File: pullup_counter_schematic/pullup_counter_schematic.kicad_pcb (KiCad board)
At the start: 2 copper layers, 75 x 45 mm, 53 parts, among them J1 FOUR_WIRE_CONN, J2 READ_PORT, Q1 MMBT3904, Q2 MMBT3904, Q3 MMBT3904, Q4 MMBT3906, SW1 SW_Push, U1 LM358, U2 HT7333, U3 P25Q40H, U4 dual_sev_seg_display, U5 AT24C02, U6 STM32F031C6Tx, Y1 32.768KHz

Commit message: Created PCB
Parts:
- removed JP1: Jumper_2_Open, Jumper:SolderJumper-2_P1.3mm_Open_RoundedPad1.0x1.5mm
- removed JP2: Jumper_3_Open, Connector_PinSocket_2.54mm:PinSocket_1x03_P2.54mm_Vertical
- removed RN1: Voltage_Divider, Potentiometer_THT:Potentiometer_Piher_PT-10-V05_Vertical
- added BT3: CR2032, Battery_Custom:CR2032_CR2025_Battery_Holder, F.Cu at (113.0, 60.0)
- added C13: 100nF, Capacitor_SMD:C_0805_2012Metric_Pad1.18x1.45mm_HandSolder, F.Cu at (125.5, 81.0)
- added C14: 100nF, Capacitor_SMD:C_0805_2012Metric_Pad1.18x1.45mm_HandSolder, F.Cu at (136.5, 82.5)
- added C15: 4.7uF, Capacitor_SMD:C_0805_2012Metric_Pad1.18x1.45mm_HandSolder, F.Cu at (137.0, 70.0)
- added C16: 1uF, Capacitor_SMD:C_0805_2012Metric_Pad1.18x1.45mm_HandSolder, F.Cu at (151.8, 95.0)
- added C17: 10pF, Capacitor_SMD:C_0603_1608Metric_Pad1.08x0.95mm_HandSolder, F.Cu at (139.0, 80.4)
- added C18: 10pF, Capacitor_SMD:C_0603_1608Metric_Pad1.08x0.95mm_HandSolder, F.Cu at (139.0, 76.1)
- added D1: D_Schottky, Diode_SMD:D_SMA_Handsoldering, F.Cu at (127.5, 48.5)
- added Q5: MMBT3906, Package_TO_SOT_SMD:SOT-23_Handsoldering, F.Cu at (145.0, 88.0)
- added R19: 47K, Resistor_SMD:R_0805_2012Metric_Pad1.20x1.40mm_HandSolder, F.Cu at (113.5, 95.0)
- added R20: 47K, Resistor_SMD:R_0805_2012Metric_Pad1.20x1.40mm_HandSolder, F.Cu at (116.5, 95.0)
- added R21: R, Resistor_SMD:R_0805_2012Metric_Pad1.20x1.40mm_HandSolder, F.Cu at (140.0, 86.5)
- added R22: R, Resistor_SMD:R_0805_2012Metric_Pad1.20x1.40mm_HandSolder, F.Cu at (140.5, 91.0)
- added R23: R, Resistor_SMD:R_0805_2012Metric_Pad1.20x1.40mm_HandSolder, F.Cu at (149.0, 93.0)
- added SW2: rst, custom_buttons_switches:TSB008, F.Cu at (125.7, 89.5)
- added SW3: start, custom_buttons_switches:TSB008, F.Cu at (131.7, 89.5)
- added SW4: TouchPad, TouchPad:TouchPad_100x100, F.Cu at (168.9, 93.3)
- added U7: STM32L051C8Tx, Package_QFP:LQFP-48_7x7mm_P0.5mm, F.Cu at (132.0, 76.0)
- added U8: KTIR0711S, pullup_counter_schematic:KTIR0711S, F.Cu at (142.7, 95.4)
- BT1: value Battery -> LR03; footprint Connector_PinHeader_2.54mm:PinHeader_1x02_P2.54mm_Vertical -> Battery_Custom:SMD_SMT_AAA_LR03; moved to B.Cu
- BT2: value Battery_Cell -> LR03; footprint Battery_Custom:CR2032_CR2025_Battery_Holder -> Battery_Custom:SMD_SMT_AAA_LR03
- C1, C5: value 1uF -> 10uF; footprint Capacitor_SMD:C_1206_3216Metric_Pad1.33x1.80mm_HandSolder -> Capacitor_SMD:C_0805_2012Metric_Pad1.18x1.45mm_HandSolder
- C10: value 10pF -> ?pF; footprint Capacitor_SMD:C_0603_1608Metric_Pad1.08x0.95mm_HandSolder -> Capacitor_SMD:C_0805_2012Metric_Pad1.18x1.45mm_HandSolder
- C11: value 10pF -> 1uF; footprint Capacitor_SMD:C_0603_1608Metric_Pad1.08x0.95mm_HandSolder -> Capacitor_SMD:C_0805_2012Metric_Pad1.18x1.45mm_HandSolder
- C12, C3, C4: footprint Capacitor_SMD:C_1206_3216Metric_Pad1.33x1.80mm_HandSolder -> Capacitor_SMD:C_0805_2012Metric_Pad1.18x1.45mm_HandSolder
- C2: value 10uF -> 100nF; footprint Capacitor_SMD:C_1206_3216Metric_Pad1.33x1.80mm_HandSolder -> Capacitor_SMD:C_0805_2012Metric_Pad1.18x1.45mm_HandSolder
- C6: value 1uF -> 100nF; footprint Capacitor_SMD:C_1206_3216Metric_Pad1.33x1.80mm_HandSolder -> Capacitor_SMD:C_0805_2012Metric_Pad1.18x1.45mm_HandSolder
- C7, C8: value 100nF -> 10uF; footprint Capacitor_SMD:C_1206_3216Metric_Pad1.33x1.80mm_HandSolder -> Capacitor_SMD:C_0805_2012Metric_Pad1.18x1.45mm_HandSolder
- C9: value 4.7uF -> 100nF; footprint Capacitor_SMD:C_1206_3216Metric_Pad1.33x1.80mm_HandSolder -> Capacitor_SMD:C_0805_2012Metric_Pad1.18x1.45mm_HandSolder
- J1: value FOUR_WIRE_CONN -> USB_B_Micro; footprint Connector_PinHeader_2.54mm:PinHeader_1x04_P2.54mm_Vertical -> Connector_USB:USB_Micro-B_Amphenol_10118194_Horizontal
- J2: value READ_PORT -> 6PinDebugPort; footprint Connector_PinSocket_2.54mm:PinSocket_2x03_P2.54mm_Vertical -> Connector_IDC:IDC-Header_2x03_P2.54mm_Vertical; moved to F.Cu
- Q1, Q2: footprint Package_TO_SOT_SMD:SOT-23 -> Package_TO_SOT_SMD:SOT-23_Handsoldering
- Q3, Q4: footprint Package_TO_SOT_SMD:SOT-23 -> Package_TO_SOT_SMD:SOT-23_Handsoldering; moved to F.Cu
- R1: value 10K -> 1K
- R12: value 1K2 -> 10K
- R13: value R -> 10K
- R14: value R -> 1K2
- R15, R16, R17, R3, R4, R5, R6, R7: moved to F.Cu
- R18: value 10K -> 47K
- R2: value R_PHOTO -> 1K; footprint OptoDevice:R_LDR_5.0x4.1mm_P3mm_Vertical -> Resistor_SMD:R_0805_2012Metric_Pad1.20x1.40mm_HandSolder
- R8, R9: value 1K -> 220R; moved to F.Cu
- SW1: value SW_Push -> boot
- U1: value LM358 -> COM_C; footprint Package_SO:SOIC-8_3.9x4.9mm_P1.27mm -> Seven_Segment_Display_Custom:2_Digit_0_56_inch
- U2: value HT7333 -> HT7325
- U3: value P25Q40H -> CH340C; footprint Package_SO:SOIC-8_3.9x4.9mm_P1.27mm -> Package_SO:SOIC-16_3.9x9.9mm_P1.27mm
- U4: value dual_sev_seg_display -> HT7325; footprint Seven_Segment_Display_Custom:2_Digit_0_56_inch -> Package_TO_SOT_SMD:SOT-89-3
- U5: value AT24C02 -> P25Q40H
- U6: value STM32F031C6Tx -> TTP223; footprint Package_QFP:LQFP-48_7x7mm_P0.5mm -> Package_TO_SOT_SMD:TSOT-23-6
- moved H1 133.5 mm to (100.0, 92.5)
- moved C6 109.4 mm to (112.0, 80.5), turned to 270 degrees
- moved C5 101.0 mm to (109.5, 80.5), turned to 270 degrees
- moved R18 100.5 mm to (110.5, 95.0), turned to 90 degrees
- moved SW1 87.5 mm to (123.2, 95.5), turned to 90 degrees
- moved C7 86.7 mm to (118.6, 40.1), turned to 270 degrees
- moved R12 81.6 mm to (126.0, 86.0)
- moved C12 81.3 mm to (126.0, 71.0), turned to 180 degrees
- moved U5 80.6 mm to (132.5, 60.5), turned to 90 degrees
- moved R10 78.9 mm to (120.3, 86.0)
- moved C11 78.0 mm to (131.5, 54.5), turned to 0 degrees
- moved C8 76.6 mm to (129.1, 40.1)
- moved Y1 76.4 mm to (143.0, 80.9)
- moved BT1 68.9 mm to (109.0, 93.0), turned to 0 degrees
- moved C9 65.9 mm to (126.6, 40.1), turned to 270 degrees
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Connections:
- BT1 pad 2: GND -> Net-(BT1-Pad2)
- BT2 pad 1: +3V0 -> Net-(BT1-Pad2)
- C1 pad 1: +3V3 -> +5V
- C11 pad 1: Net-(C11-Pad1) -> VCC
- C12 pad 1: +3V0 -> VCC
- C2 pad 1: +BATT -> +5V
- C3 pad 1: +3V3 -> +BATT
- C4 pad 1: +3V3 -> Net-(C4-Pad1)
- C5 pad 1: /~HOLD -> VCC
- C6 pad 1: +3V3 -> VCC
- C7 pad 1: +3V3 -> +3V0
- C8 pad 1: +3V3 -> /V_BACKUP
- C9 pad 1: +3V3 -> /V_BACKUP
- J1 pad 1: GND -> +5V
- J1 pad 2: /SWCLK -> Net-(J1-Pad2)
- J1 pad 3: /SWDIO -> Net-(J1-Pad3)
- J1 pad 4: +3V3 -> GND
- J2 pad 1: /READ_PWR -> GND
- J2 pad 2: /MOSI -> /SWCLK
- J2 pad 3: /~CE -> /SWDIO
- J2 pad 4: /SCK -> /~RST
- J2 pad 5: /MISO -> (no net)
- J2 pad 6: GND -> VCC
- Q4 pad 2: Net-(Q4-Pad2) -> +BATT
- Q4 pad 3: +BATT -> Net-(Q4-Pad3)
- R1 pad 1: +3V3 -> Net-(R1-Pad1)
- R1 pad 2: /DIST_OUTA -> /dis_a
- R12 pad 1: Net-(Q2-Pad1) -> VCC
- R12 pad 2: /dis_sel_0 -> /~RST
- R13 pad 1: Net-(R13-Pad1) -> VCC
- R13 pad 2: /DIST_REF -> /Start
- R14 pad 1: /DIST_OUTD -> Net-(Q2-Pad1)
- R14 pad 2: Net-(R13-Pad1) -> /dis_sel_0
- R15 pad 1: Net-(Q3-Pad1) -> +5V
- R15 pad 2: /BAT_SENSE_EN -> /USB_FLAG
- R16 pad 1: /BAT_SENSE -> /USB_FLAG
- R16 pad 2: Net-(Q4-Pad2) -> GND
- R17 pad 1: GND -> Net-(Q3-Pad1)
- R17 pad 2: /BAT_SENSE -> /BAT_SENSE_EN
- R18 pad 1: +3V3 -> +BATT
- R18 pad 2: /~RST -> Net-(Q3-Pad3)
- R2 pad 1: /DIST_OUTA -> Net-(R2-Pad1)
- R2 pad 2: GND -> /dis_b
- R3 pad 2: /dis_a -> /dis_c
- R4 pad 2: /dis_b -> /dis_d
- R5 pad 2: /dis_c -> /dis_e
- R6 pad 2: /dis_d -> /dis_f
- R7 pad 2: /dis_e -> /dis_g
- R8 pad 1: Net-(R8-Pad1) -> Net-(J1-Pad3)
- R8 pad 2: /dis_f -> /USB_DP
- R9 pad 1: Net-(R9-Pad1) -> /USB_DM
- R9 pad 2: /dis_g -> Net-(J1-Pad2)
- SW1 pad 1: /~RST -> VCC
- SW1 pad 2: GND -> /boot
- U1 pad 1: /DIST_OUTD -> Net-(R3-Pad1)
- U1 pad 2: /DIST_OUTA -> (no net)
- U1 pad 3: Net-(R13-Pad1) -> Net-(R5-Pad1)
- U1 pad 4: GND -> Net-(R4-Pad1)
- U1 pad 5: GND -> Net-(R7-Pad1)
- U1 pad 6: GND -> Net-(R6-Pad1)
- U1 pad 7: (no net) -> /disp_pwr_0
- U1 pad 8: +3V3 -> /disp_pwr_1
- U2 pad 3: +3V3 -> VCC
- U3 pad 1: /~CE -> GND
- U3 pad 2: /MISO -> /MCU_RX
- U3 pad 3: /~HOLD -> /MCU_TX
- U3 pad 4: GND -> Net-(C4-Pad1)
- U3 pad 5: /MOSI -> /USB_DP
- U3 pad 6: /SCK -> /USB_DM
- U3 pad 7: /~HOLD -> (no net)
- U3 pad 8: /~HOLD -> (no net)
- U4 pad 1: Net-(R5-Pad1) -> GND
- U4 pad 2: (no net) -> +3V0
- U4 pad 3: Net-(R7-Pad1) -> /V_BACKUP
- U5 pad 1: GND -> /~CE
- U5 pad 2: GND -> /MISO
- U5 pad 3: GND -> VCC
- U5 pad 5: /SDA -> /MOSI
- U5 pad 6: /SCL -> /SCK
- U5 pad 7: GND -> VCC
- U5 pad 8: +3V3 -> VCC
- U6 pad 1: +3V0 -> /TouchPin
- U6 pad 2: (no net) -> GND
- U6 pad 4: Net-(C11-Pad1) -> GND
- U6 pad 5: (no net) -> VCC
- U6 pad 6: (no net) -> GND
- Y1 pad 1: Net-(C10-Pad1) -> Net-(C17-Pad1)
- Y1 pad 2: Net-(C11-Pad1) -> Net-(C18-Pad1)
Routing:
- net VCC: track 0.00 -> 193.1 mm, vias 0 -> 5
- net +3V3: track 154.5 -> 0.00 mm, vias 2 -> 0
- net /dis_sel_0: track 25.2 -> 84.3 mm, vias 0 -> 2
- net /dis_f: track 20.6 -> 74.5 mm, vias 1 -> 2
- net /~RST: track 18.7 -> 69.5 mm, vias 4 -> 3
- net Net-(BT1-Pad2): track 0.00 -> 50.6 mm
- net /~HOLD: track 46.2 -> 0.00 mm, vias 2 -> 0
- net /dis_sel_1: track 31.9 -> 77.8 mm, vias 0 -> 2
- net /dis_g: track 19.6 -> 62.2 mm, vias 1 -> 2
- net /dis_b: track 29.2 -> 70.4 mm, vias 1 -> 2
- net /USB_FLAG: track 0.00 -> 40.7 mm, vias 0 -> 2
- net /dis_d: track 22.4 -> 58.6 mm, vias 1 -> 2
- net /dis_a: track 31.2 -> 66.1 mm, vias 1 -> 2
- net /MISO: track 42.9 -> 9.69 mm, vias 3 -> 0
- net /TouchPin: track 0.00 -> 32.7 mm, vias 0 -> 4
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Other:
- board size 75 x 45 mm -> 95 x 65 mm
- board text added: "BOOT"
- board text added: "Otwory M3"
- board text added: "START"
- board text removed: "+ -"
- board text removed: "Debug Port"
- board text removed: "Flash Read Port"
- board text removed: "GND"
- board text removed: "JLCJLCJLCJLC"
- board text removed: "MOSI/SCK/GND VCC/~CE~/MISO"
- board text removed: "Normal Operation"
- board text removed: "Pull-up Counter - v01 - by Mkrysz"
- board text removed: "Read Data"
- board text removed: "SWCLK"
- board text removed: "SWDIO"
- board text removed: "VCC"
- board text removed: "boot jumper"

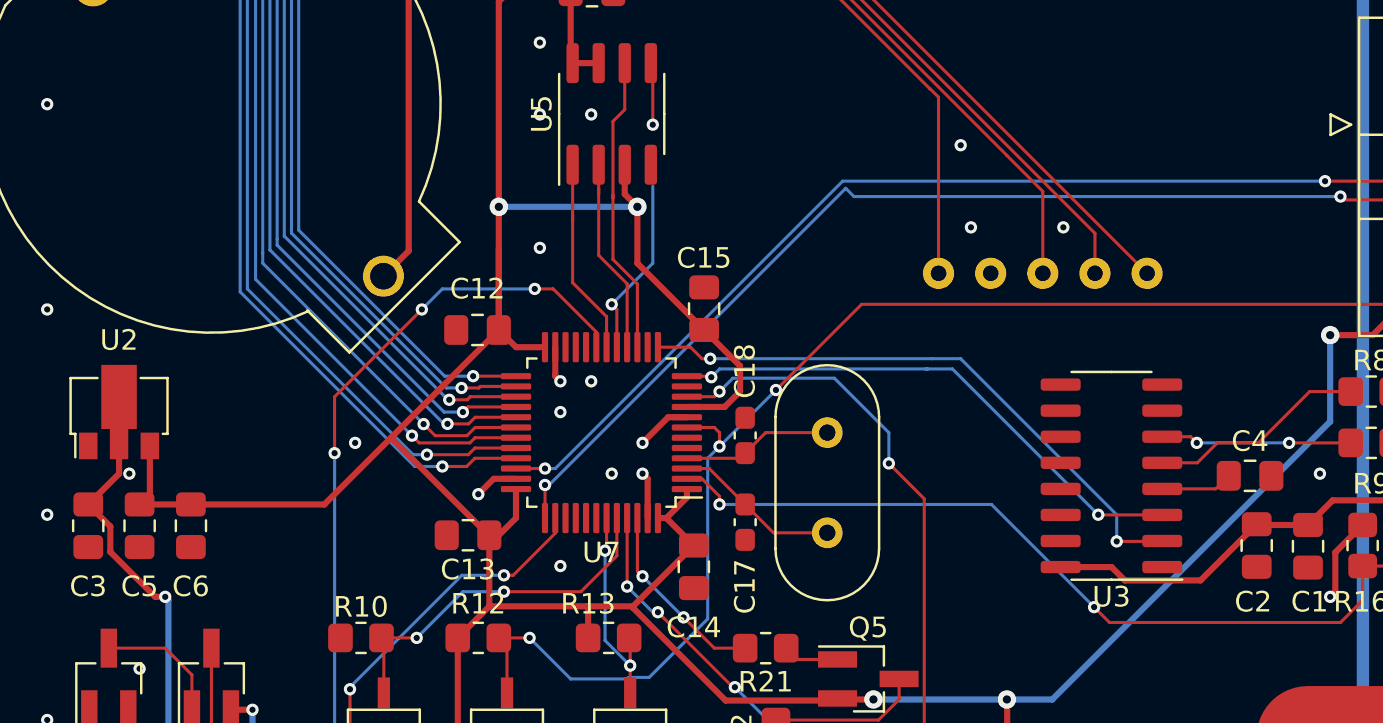
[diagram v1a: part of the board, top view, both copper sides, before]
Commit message: Runned DRC and fixed some problems
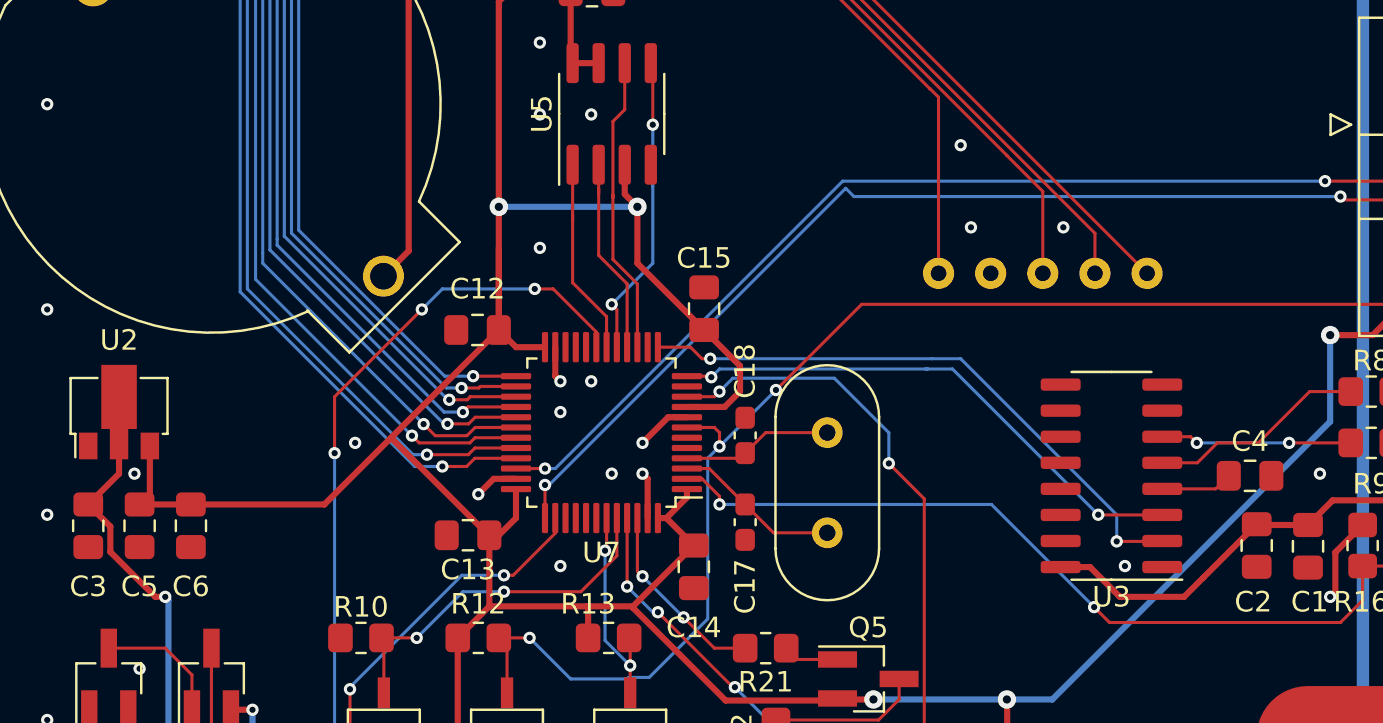
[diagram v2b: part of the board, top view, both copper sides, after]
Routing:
- net /MOSI: track 11.8 -> 14.8 mm
- net +5V: track 23.6 -> 24.3 mm
- net GND: vias 38 -> 39

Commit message: Generated PCB's Gerbers
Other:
- board text added: "JLCJLCJLCJLC"
- board text added: "Pull-up Counter V02 By MKrysz"

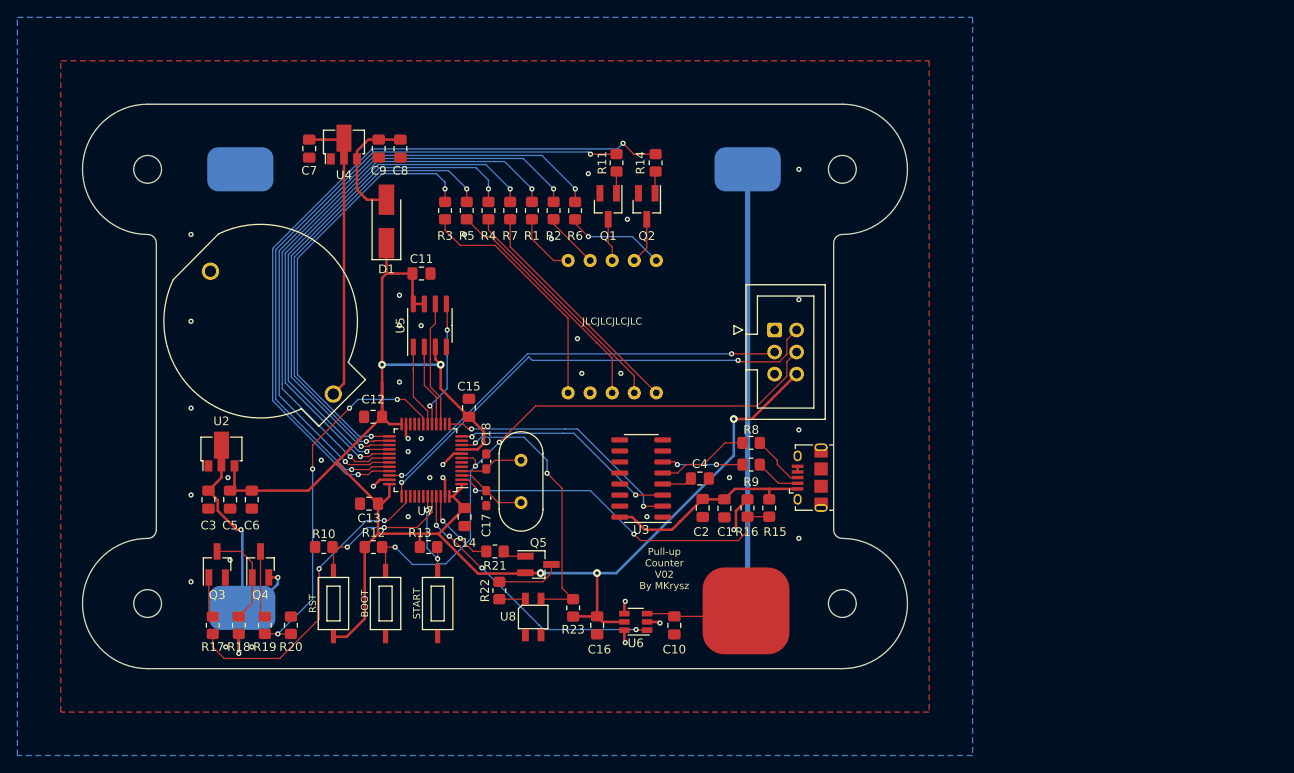
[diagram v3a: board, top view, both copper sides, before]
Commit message: Added step-up, SD-Card, OLED display and changed MCU
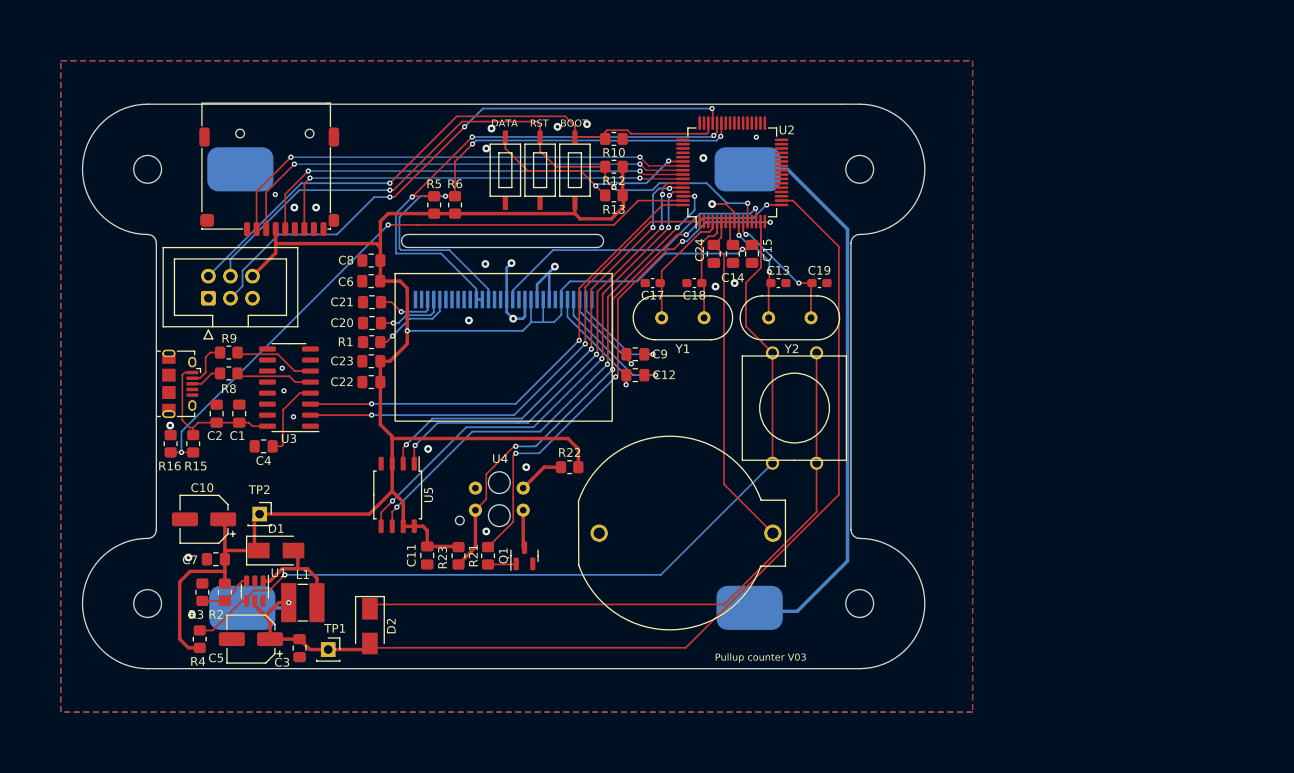
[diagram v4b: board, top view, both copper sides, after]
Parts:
- removed C16: 1uF, Capacitor_SMD:C_0805_2012Metric_Pad1.18x1.45mm_HandSolder
- removed Q2, Q3: MMBT3904, Package_TO_SOT_SMD:SOT-23_Handsoldering
- removed Q4, Q5: MMBT3906, Package_TO_SOT_SMD:SOT-23_Handsoldering
- removed R11, R14: 1K2, Resistor_SMD:R_0805_2012Metric_Pad1.20x1.40mm_HandSolder
- removed R17, R18, R19, R20: 47K, Resistor_SMD:R_0805_2012Metric_Pad1.20x1.40mm_HandSolder
- removed R7: 1K, Resistor_SMD:R_0805_2012Metric_Pad1.20x1.40mm_HandSolder
- removed U6: TTP223, Package_TO_SOT_SMD:TSOT-23-6
- removed U7: STM32L051C8Tx, Package_QFP:LQFP-48_7x7mm_P0.5mm
- removed U8: KTIR0711S, pullup_counter_schematic:KTIR0711S
- added C19: 20pF, Capacitor_SMD:C_0603_1608Metric_Pad1.08x0.95mm_HandSolder, F.Cu at (177.4, 55.6)
- added C20: 10uF, Capacitor_SMD:C_0805_2012Metric_Pad1.18x1.45mm_HandSolder, F.Cu at (125.8, 60.2)
- added C21: 10uF, Capacitor_SMD:C_0805_2012Metric_Pad1.18x1.45mm_HandSolder, F.Cu at (125.8, 57.8)
- added C22: 10uF, Capacitor_SMD:C_0805_2012Metric_Pad1.18x1.45mm_HandSolder, F.Cu at (125.8, 67.0)
- added C23: 100nF, Capacitor_SMD:C_0805_2012Metric_Pad1.18x1.45mm_HandSolder, F.Cu at (125.8, 64.6)
- added C24: 100nF, Capacitor_SMD:C_0805_2012Metric_Pad1.18x1.45mm_HandSolder, F.Cu at (165.2, 52.2)
- added D2: SS14, Diode_SMD:D_SMA, F.Cu at (125.6, 95.1)
- added DS1: OLED-128O064D, Display:OLED-128O064D, F.Cu at (141.0, 57.5)
- added J3: Micro_SD_Card, uSD_socket:uSD_socket, F.Cu at (117.0, 45.9)
- added L1: 4.7uH, Inductor_SMD:L_Ferrocore_DLG-0403, F.Cu at (117.9, 92.4)
- added TP1: ~, Connector_PinSocket_2.54mm:PinSocket_1x01_P2.54mm_Vertical, F.Cu at (120.8, 97.8)
- added TP2: ~, Connector_PinSocket_2.54mm:PinSocket_1x01_P2.54mm_Vertical, F.Cu at (112.9, 82.2)
- added Y2: 8MHz, Crystal:Crystal_HC49-4H_Vertical, F.Cu at (171.5, 59.6)
- C10: value ?pF -> 22uF; footprint Capacitor_SMD:C_0805_2012Metric_Pad1.18x1.45mm_HandSolder -> Capacitor_SMD:CP_Elec_5x4.5
- C12, C9: value 100nF -> 2.2uF
- C13: value 100nF -> 20pF; footprint Capacitor_SMD:C_0805_2012Metric_Pad1.18x1.45mm_HandSolder -> Capacitor_SMD:C_0603_1608Metric_Pad1.08x0.95mm_HandSolder
- C3, C7, C8: value 10uF -> 100nF
- C5: value 10uF -> 22uF; footprint Capacitor_SMD:C_0805_2012Metric_Pad1.18x1.45mm_HandSolder -> Capacitor_SMD:CP_Elec_5x4.5
- C6: value 100nF -> 10uF
- D1: value D_Schottky -> SS14; footprint Diode_SMD:D_SMA_Handsoldering -> Diode_SMD:D_SMA
- Q1: footprint Package_TO_SOT_SMD:SOT-23_Handsoldering -> Package_TO_SOT_SMD:SOT-23
- R1: value 1K -> 390K
- R2, R3: value 1K -> R
- R21: value R -> 1K2
- R22: value R -> 220R
- R23: value R -> 22K
- R4: value 1K -> 10K
- R5, R6: value 1K -> 4K7
- SW3: value start -> dataDump
- SW4: value TouchPad -> start; footprint TouchPad:TouchPad_100x100 -> custom_buttons_switches:sw_push_12_x_12_mm
- U1: value COM_C -> MT3608; footprint Seven_Segment_Display_Custom:2_Digit_0_56_inch -> Package_TO_SOT_SMD:SOT-23-6
- U2: value HT7325 -> STM32G070RBT6; footprint Package_TO_SOT_SMD:SOT-89-3 -> Package_QFP:LQFP-64_10x10mm_P0.5mm
- U4: value HT7325 -> TCRT5000; footprint Package_TO_SOT_SMD:SOT-89-3 -> TCRT5000:TCRT5000
- U5: value P25Q40H -> W25Q80; footprint Package_SO:SOIC-8_3.9x4.9mm_P1.27mm -> Package_SO:SOIC-8_5.275x5.275mm_P1.27mm
- moved J1 73.3 mm to (103.8, 67.2), turned to -90 degrees
- moved U2 67.0 mm to (167.3, 42.9)
- moved R16 66.8 mm to (102.7, 74.1)
- moved R15 66.7 mm to (105.2, 74.1)
- moved J2 65.3 mm to (107.0, 57.3), turned to 90 degrees
- moved R9 61.5 mm to (109.3, 63.6), turned to 180 degrees
- moved R8 60.7 mm to (109.3, 66.0), turned to 0 degrees
- moved R4 59.5 mm to (106.0, 96.6)
- moved R2 58.0 mm to (108.9, 91.2), turned to -90 degrees
- moved R10 57.7 mm to (153.7, 39.0), turned to 0 degrees
- moved SW1 57.1 mm to (151.0, 45.6)
- moved C2 57.0 mm to (107.9, 70.6), turned to 90 degrees
- moved C1 56.9 mm to (110.5, 70.6), turned to 90 degrees
- moved C10 55.5 mm to (106.5, 82.8), turned to 180 degrees
- moved C13 53.5 mm to (172.6, 55.6), turned to 0 degrees
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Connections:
- BT1 pad 1: +BATT -> /BAT_RAW
- BT3 pad 1: +3V0 -> +BATT
- C10 pad 1: Net-(C10-Pad1) -> VCC
- C12 pad 1: VCC -> Net-(C12-Pad1)
- C12 pad 2: GND -> Net-(C12-Pad2)
- C13 pad 1: VCC -> /OSC_IN
- C17 pad 1: Net-(C17-Pad1) -> /OSC32_IN
- C18 pad 1: Net-(C18-Pad1) -> /OSC32_OUT
- C3 pad 1: +BATT -> /BAT_RAW
- C5 pad 1: VCC -> /BAT_RAW
- C7 pad 1: +3V0 -> VCC
- C8 pad 1: /V_BACKUP -> VCC
- C9 pad 1: /V_BACKUP -> Net-(C9-Pad1)
- C9 pad 2: GND -> Net-(C9-Pad2)
- D1 pad 2: /V_BACKUP -> Net-(D1-Pad2)
- J2 pad 4: /~RST -> /~{RST}
- J2 pad 5: (no net) -> unconnected-(J2-Pad5)
- Q1 pad 3: /disp_pwr_1 -> Net-(Q1-Pad3)
- R1 pad 1: Net-(R1-Pad1) -> Net-(DS1-Pad26)
- R1 pad 2: /dis_a -> GND
- R10 pad 1: /boot -> /SWCLK
- R12 pad 2: /~RST -> /~{RST}
- R13 pad 2: /Start -> /dataDump
- R2 pad 1: Net-(R2-Pad1) -> VCC
- R2 pad 2: /dis_b -> /PWR_FB
- R21 pad 1: Net-(Q5-Pad1) -> Net-(Q1-Pad1)
- R21 pad 2: /DISTANCE_EN -> /PROX_EN
- R22 pad 2: Net-(Q5-Pad3) -> VCC
- R23 pad 2: /DISTANCE -> /PROX_OUT
- R3 pad 1: Net-(R3-Pad1) -> /PWR_FB
- R3 pad 2: /dis_c -> GND
- R4 pad 1: Net-(R4-Pad1) -> VCC
- R4 pad 2: /dis_d -> /PWR_EN
- R5 pad 1: Net-(R5-Pad1) -> VCC
- R5 pad 2: /dis_e -> /SDA
- R6 pad 1: Net-(R6-Pad1) -> VCC
- R6 pad 2: /dis_f -> /SCK
- SW1 pad 2: /boot -> /SWCLK
- SW2 pad 1: /~RST -> /~{RST}
- SW3 pad 1: /Start -> /dataDump
- SW4 pad 1: Net-(C10-Pad1) -> Net-(D2-Pad1)
- U1 pad 1: Net-(R3-Pad1) -> Net-(D1-Pad2)
- U1 pad 2: (no net) -> GND
- U1 pad 3: Net-(R5-Pad1) -> /PWR_FB
- U1 pad 4: Net-(R4-Pad1) -> /PWR_EN
- U1 pad 5: Net-(R7-Pad1) -> /BAT_RAW
- U1 pad 6: Net-(R6-Pad1) -> unconnected-(U1-Pad6)
- U2 pad 1: GND -> /MCU_RX
- U2 pad 2: +BATT -> unconnected-(U2-Pad2)
- U2 pad 3: VCC -> unconnected-(U2-Pad3)
- U3 pad 10: (no net) -> unconnected-(U3-Pad10)
- U3 pad 11: (no net) -> unconnected-(U3-Pad11)
- U3 pad 12: (no net) -> unconnected-(U3-Pad12)
- U3 pad 13: (no net) -> unconnected-(U3-Pad13)
- U3 pad 14: (no net) -> unconnected-(U3-Pad14)
- U3 pad 15: (no net) -> unconnected-(U3-Pad15)
- U3 pad 7: (no net) -> unconnected-(U3-Pad7)
- U3 pad 8: (no net) -> unconnected-(U3-Pad8)
- U3 pad 9: (no net) -> unconnected-(U3-Pad9)
- U4 pad 1: GND -> /PROX_OUT
- U4 pad 2: +3V0 -> GND
- U4 pad 3: /V_BACKUP -> Net-(R22-Pad1)
- U5 pad 1: /~CE -> /MEM_~{CE}
- U5 pad 2: /MISO -> /MEM_MISO
- U5 pad 5: /MOSI -> /MEM_MOSI
- U5 pad 6: /SCK -> /MEM_SCK
- Y1 pad 1: Net-(C17-Pad1) -> /OSC32_IN
- Y1 pad 2: Net-(C18-Pad1) -> /OSC32_OUT
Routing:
- net /BAT_RAW: track 0.00 -> 124.9 mm, vias 0 -> 1
- net /PWR_EN: track 0.00 -> 104.0 mm, vias 0 -> 1
- net /dis_sel_0: track 84.3 -> 0.00 mm, vias 2 -> 0
- net /dis_sel_1: track 77.8 -> 0.00 mm, vias 2 -> 0
- net /~{RST}: track 0.00 -> 77.4 mm, vias 0 -> 3
- net /dis_f: track 74.5 -> 0.00 mm, vias 2 -> 0
- net Net-(D2-Pad1): track 0.00 -> 74.2 mm
- net /dis_b: track 70.4 -> 0.00 mm, vias 2 -> 0
- net /~RST: track 69.5 -> 0.00 mm, vias 3 -> 0
- net /dis_a: track 66.1 -> 0.00 mm, vias 2 -> 0
- net /PROX_OUT: track 0.00 -> 63.3 mm, vias 0 -> 4
- net /dis_g: track 62.2 -> 0.00 mm, vias 2 -> 0
- net /SDA: track 0.00 -> 62.0 mm, vias 0 -> 3
- net /dis_d: track 58.6 -> 0.00 mm, vias 2 -> 0
- net /MEM_SCK: track 0.00 -> 58.3 mm, vias 0 -> 4
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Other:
- board size 95 x 65 mm -> 97 x 65 mm
- net class Default removed
- board text added: "DATA"
- board text added: "Pullup counter V03"
- board text removed: "JLCJLCJLCJLC"
- board text removed: "Pull-up Counter V02 By MKrysz"
- board text removed: "START"

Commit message: Changed proximity sens to SMD, added more USR btns
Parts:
- removed R13: 10K, Resistor_SMD:R_0805_2012Metric_Pad1.20x1.40mm_HandSolder
- added SW5: UsrBtn1, custom_buttons_switches:TSB008, F.Cu at (131.3, 39.6)
- added SW6: UsrBtn2, custom_buttons_switches:TSB008, F.Cu at (135.3, 39.6)
- added SW7: UsrBtn3, custom_buttons_switches:TSB008, F.Cu at (127.3, 39.5)
- SW3: value dataDump -> UsrBtn0
- U4: value TCRT5000 -> ITR8307; footprint TCRT5000:TCRT5000 -> OptoDevice:Everlight_ITR8307
- moved R5 21.5 mm to (153.8, 41.0), turned to 180 degrees
- moved R6 18.7 mm to (153.8, 43.2), turned to 180 degrees
- moved R10 6.20 mm to (159.5, 36.8), turned to -90 degrees
- moved R12 3.30 mm to (153.7, 45.5)
- moved U4 2.92 mm to (140.2, 80.2), turned to -90 degrees
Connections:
- net /dataDump renamed /UsrBtn0
- U2 pad 51: unconnected-(U2-Pad51) -> /UsrBtn3
- U2 pad 52: unconnected-(U2-Pad52) -> /UsrBtn2
- U2 pad 53: unconnected-(U2-Pad53) -> /UsrBtn1
- U4 pad 1: /PROX_OUT -> Net-(Q1-Pad3)
- U4 pad 2: GND -> Net-(R22-Pad1)
- U4 pad 3: Net-(R22-Pad1) -> /PROX_OUT
- U4 pad 4: Net-(Q1-Pad3) -> GND
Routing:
- net /UsrBtn3: track 0.00 -> 34.9 mm, vias 0 -> 2
- net /UsrBtn2: track 0.00 -> 30.6 mm, vias 0 -> 2
- net /UsrBtn1: track 0.00 -> 26.2 mm, vias 0 -> 2
- net Net-(Q1-Pad3): track 4.37 -> 10.00 mm
- net /UsrBtn0: track 26.4 -> 21.6 mm
- net /PROX_OUT: track 63.3 -> 67.4 mm
- net /SCK: track 61.8 -> 65.8 mm, vias 3 -> 4
- net VCC: track 229.1 -> 231.0 mm
- net /SDA: track 62.0 -> 63.8 mm, vias 3 -> 4
- net /~{RST}: track 77.4 -> 78.4 mm
- net GND: vias 26 -> 37
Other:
- board text added: "USR0"
- board text added: "USR1"
- board text added: "USR2"
- board text added: "USR3"
- board text removed: "DATA"
